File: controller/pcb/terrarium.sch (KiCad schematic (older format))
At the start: 72 parts, among them K1 G3MB-202P, K2 G3MB-202P, K3 G3MB-202P, P1 USB_C_Plug_USB2.0, Q1 S8050, Q2 S8050, Q3 S8050, Q4 S8050, SW1 RESET, SW3 RTC BATTERY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

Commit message: update footprints, move rx/tx leds
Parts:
- removed R12: 5k, Resistor_SMD:R_1206_3216Metric, symbol Device:R_Small
- removed SW3: RTC BATTERY, Button_Switch_SMD:SW_DIP_SPSTx01_Slide_6.7x4.1mm_W6.73mm_P2.54mm_LowProfile_JPin, symbol Switch:SW_Push
- LED4: value POWER -> PWR
- LED5: value SENS -> SNS
- R12: renamed from R19; value 10k -> 3k
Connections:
- wire segments 211 -> 205
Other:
- moved on the sheet: LED4, LED6, LED7, R12
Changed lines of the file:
@@
 Wire Wire Line
 	4350 4600 4250 4600
-$Comp
-L Mechanical:MountingHole H1
-U 1 1 61A0FEAA
-P 900 6300
-F 0 "H1" H 1000 6300 50  0000 L CNN
-F 1 "MountingHole" H 1000 6255 50  0001 L CNN
-F 2 "MountingHole:MountingHole_3.2mm_M3_Pad_Via" H 900 6300 50  0001 C CNN
-F 3 "~" H 900 6300 50  0001 C CNN
-	1    900  6300
-	1    0    0    -1
-$EndComp
-$Comp
-L Mechanical:MountingHole H2
-U 1 1 61A115E3
-P 1300 6300
-F 0 "H2" H 1400 6300 50  0000 L CNN
-F 1 "MountingHole" H 1400 6255 50  0001 L CNN
-F 2 "MountingHole:MountingHole_3.2mm_M3_Pad_Via" H 1300 6300 50  0001 C CNN
-F 3 "~" H 1300 6300 50  0001 C CNN
-	1    1300 6300
-	1    0    0    -1
-$EndComp
-$Comp
-L Mechanical:MountingHole H3
-U 1 1 61A11970
-P 1700 6300
-F 0 "H3" H 1800 6300 50  0000 L CNN
-F 1 "MountingHole" H 1800 6255 50  0001 L CNN
-F 2 "MountingHole:MountingHole_3.2mm_M3_Pad_Via" H 1700 6300 50  0001 C CNN
-F 3 "~" H 1700 6300 50  0001 C CNN
-	1    1700 6300
-	1    0    0    -1
-$EndComp
-$Comp
-L Mechanical:MountingHole H4
-U 1 1 61A11DAB
-P 2100 6300
-F 0 "H4" H 2200 6300 50  0000 L CNN
-F 1 "MountingHole" H 2200 6255 50  0001 L CNN
-F 2 "MountingHole:MountingHole_3.2mm_M3_Pad_Via" H 2100 6300 50  0001 C CNN
-F 3 "~" H 2100 6300 50  0001 C CNN
-	1    2100 6300
-	1    0    0    -1
-$EndComp
-Text Notes 700  6050 0    50   ~ 0
-Mount holes
 Text Notes 3050 650  0    50   ~ 0
 Relays
@@
 	1    0    0    -1
 $EndComp
-Wire Wire Line
-	10100 5500 10400 5500
 Wire Wire Line
 	11000 6750 10100 6750
@@
 $EndComp
 $Comp
-L Switch:SW_Push SW3
-U 1 1 61C4BD91
-P 10600 5500
-F 0 "SW3" H 10600 5785 50  0000 C CNN
-F 1 "RTC BATTERY" H 10600 5694 50  0000 C CNN
-F 2 "Button_Switch_SMD:SW_DIP_SPSTx01_Slide_6.7x4.1mm_W6.73mm_P2.54mm_LowProfile_JPin" H 10600 5700 50  0001 C CNN
-F 3 "~" H 10600 5700 50  0001 C CNN
-	1    10600 5500
-	1    0    0    -1
-$EndComp
-$Comp
 L Device:Q_NPN_BEC Q3
 U 1 1 61BD2EC2
@@
 G33
 Wire Wire Line
-	10800 5500 11000 5500
-Wire Wire Line
 	11000 5500 11000 5800
 Wire Wire Line
@@
 Connection ~ 10100 5500
 Wire Notes Line
-	700  6100 700  6500
-Wire Notes Line
-	700  6500 2400 6500
-Wire Notes Line
-	2400 6500 2400 6100
-Wire Notes Line
-	700  6100 2400 6100
-Wire Notes Line
 	700  6800 2200 6800
 Wire Notes Line
@@
 	2200 8150 700  8150
 Wire Notes Line
-	8450 4700 8450 700
+	7700 4700 7700 700
 Text Notes 8450 650  0    50   ~ 0
 ESP32 WROOM 32
@@
 $EndComp
 Wire Wire Line
-	4550 9100 4550 9400
-Connection ~ 4550 9100
-Connection ~ 3850 9100
-Wire Wire Line
-	3850 9100 4550 9100
-Wire Wire Line
-	4250 9950 4550 9950
-Wire Wire Line
-	4550 9000 4550 9100
-Wire Wire Line
-	3850 9950 4050 9950
-Connection ~ 3850 9950
-Wire Wire Line
 	3850 9600 3850 9950
-Wire Wire Line
-	4550 9950 4550 9700
 Wire Wire Line
 	3300 9950 3850 9950
@@
 L power:+3V3 #PWR010
 U 1 1 61CB24C1
-P 4550 9000
-F 0 "#PWR010" H 4550 8850 50  0001 C CNN
-F 1 "+3V3" H 4565 9173 50  0000 C CNN
-F 2 "" H 4550 9000 50  0001 C CNN
-F 3 "" H 4550 9000 50  0001 C CNN
-	1    4550 9000
+P 3850 9100
+F 0 "#PWR010" H 3850 8950 50  0001 C CNN
+F 1 "+3V3" H 3865 9273 50  0000 C CNN
+F 2 "" H 3850 9100 50  0001 C CNN
+F 3 "" H 3850 9100 50  0001 C CNN
+	1    3850 9100
 	-1   0    0    -1
 $EndComp
@@
 L Device:LED LED4
 U 1 1 61C6039A
-P 4550 9550
-F 0 "LED4" H 4650 9450 50  0000 R CNN
-F 1 "POWER" H 4650 9650 50  0000 R CNN
-F 2 "LED_SMD:LED_1206_3216Metric" H 4550 9550 50  0001 C CNN
-F 3 "~" H 4550 9550 50  0001 C CNN
-	1    4550 9550
-	0    -1   -1   0
-$EndComp
-$Comp
-L Device:R_Small R12
-U 1 1 61C5EFC3
-P 4150 9950
-F 0 "R12" V 4250 9950 50  0000 C CNN
-F 1 "5k" V 4050 9950 50  0000 C CNN
-F 2 "Resistor_SMD:R_1206_3216Metric" H 4150 9950 50  0001 C CNN
-F 3 "~" H 4150 9950 50  0001 C CNN
-	1    4150 9950
+P 8300 3200
+F 0 "LED4" H 8400 3100 50  0000 R CNN
+F 1 "PWR" H 8400 3300 50  0000 R CNN
+F 2 "LED_SMD:LED_1206_3216Metric" H 8300 3200 50  0001 C CNN
+F 3 "~" H 8300 3200 50  0001 C CNN
+	1    8300 3200
 	0    -1   -1   0
 $EndComp
@@
 P 8650 8150
 F 0 "LED5" H 8750 8050 50  0000 R CNN
-F 1 "SENS" H 8750 8250 50  0000 R CNN
+F 1 "SNS" H 8750 8250 50  0000 R CNN
 F 2 "LED_SMD:LED_1206_3216Metric" H 8650 8150 50  0001 C CNN
 F 3 "~" H 8650 8150 50  0001 C CNN
@@
 L Device:LED LED6
 U 1 1 6243730D
-P 8700 2500
-F 0 "LED6" H 8800 2400 50  0000 R CNN
-F 1 "RX" H 8800 2600 50  0000 R CNN
-F 2 "LED_SMD:LED_1206_3216Metric" H 8700 2500 50  0001 C CNN
-F 3 "~" H 8700 2500 50  0001 C CNN
-	1    8700 2500
+P 9100 3200
+F 0 "LED6" H 9200 3100 50  0000 R CNN
+F 1 "RX" H 9200 3300 50  0000 R CNN
+F 2 "LED_SMD:LED_1206_3216Metric" H 9100 3200 50  0001 C CNN
+F 3 "~" H 9100 3200 50  0001 C CNN
+	1    9100 3200
 	0    -1   -1   0
 $EndComp
@@
 L Device:LED LED7
 U 1 1 62438D58
-P 9100 2500
-F 0 "LED7" H 9200 2400 50  0000 R CNN
-F 1 "TX" H 9200 2600 50  0000 R CNN
-F 2 "LED_SMD:LED_1206_3216Metric" H 9100 2500 50  0001 C CNN
-F 3 "~" H 9100 2500 50  0001 C CNN
-	1    9100 2500
-	0    -1   -1   0
-$EndComp
-Text GLabel 8700 2350 1    50   Input ~ 0
+P 8700 3200
+F 0 "LED7" H 8800 3100 50  0000 R CNN
+F 1 "TX" H 8800 3300 50  0000 R CNN
+F 2 "LED_SMD:LED_1206_3216Metric" H 8700 3200 50  0001 C CNN
+F 3 "~" H 8700 3200 50  0001 C CNN
+	1    8700 3200
+	0    -1   -1   0
+$EndComp
+Text GLabel 9100 3350 3    50   Input ~ 0
 RX
-Text GLabel 9100 2350 1    50   Input ~ 0
+Text GLabel 8700 3350 3    50   Input ~ 0
 TX
 Wire Wire Line
-	8700 2650 8700 2850
-Wire Wire Line
-	8700 2850 8900 2850
-Wire Wire Line
-	9100 2850 9100 2650
-$Comp
-L Device:R_Small R19
+	9100 3050 9100 2850
+Wire Wire Line
+	8700 2850 8700 3050
+$Comp
+L Device:R_Small R12
 U 1 1 624CEFE7
-P 8900 3050
-F 0 "R19" V 9000 3050 50  0000 C CNN
-F 1 "10k" V 8800 3050 50  0000 C CNN
-F 2 "Resistor_SMD:R_1206_3216Metric" H 8900 3050 50  0001 C CNN
-F 3 "~" H 8900 3050 50  0001 C CNN
-	1    8900 3050
-	-1   0    0    1
-$EndComp
-Wire Wire Line
-	8900 2950 8900 2850
-Connection ~ 8900 2850
-Wire Wire Line
-	8900 2850 9100 2850
-$Comp
-L power:GND #PWR023
-U 1 1 624FB737
-P 8900 3300
-F 0 "#PWR023" H 8900 3050 50  0001 C CNN
-F 1 "GND" H 8905 3127 50  0000 C CNN
-F 2 "" H 8900 3300 50  0001 C CNN
-F 3 "" H 8900 3300 50  0001 C CNN
-	1    8900 3300
-	1    0    0    -1
-$EndComp
-Wire Wire Line
-	8900 3300 8900 3150
+P 8700 2650
+F 0 "R12" V 8800 2650 50  0000 C CNN
+F 1 "3k" V 8600 2650 50  0000 C CNN
+F 2 "Resistor_SMD:R_1206_3216Metric" H 8700 2650 50  0001 C CNN
+F 3 "~" H 8700 2650 50  0001 C CNN
+	1    8700 2650
+	1    0    0    -1
+$EndComp
+Wire Wire Line
+	8700 2750 8700 2850
+Wire Wire Line
+	8700 2400 8700 2550
+$Comp
+L power:+3V3 #PWR0101
+U 1 1 61EFC8AF
+P 8700 2400
+F 0 "#PWR0101" H 8700 2250 50  0001 C CNN
+F 1 "+3V3" H 8715 2573 50  0000 C CNN
+F 2 "" H 8700 2400 50  0001 C CNN
+F 3 "" H 8700 2400 50  0001 C CNN
+	1    8700 2400
+	-1   0    0    -1
+$EndComp
+Wire Wire Line
+	10100 5500 11000 5500
+Connection ~ 3850 9100
+Wire Wire Line
+	8700 2850 8300 2850
+Wire Wire Line
+	8300 2850 8300 3050
+Connection ~ 8700 2850
+$Comp
+L power:GND #PWR0102
+U 1 1 62065A46
+P 8300 3350
+F 0 "#PWR0102" H 8300 3100 50  0001 C CNN
+F 1 "GND" H 8305 3177 50  0000 C CNN
+F 2 "" H 8300 3350 50  0001 C CNN
+F 3 "" H 8300 3350 50  0001 C CNN
+	1    8300 3350
+	1    0    0    -1
+$EndComp
+Wire Wire Line
+	8700 2850 9100 2850
+Wire Notes Line
+	700  6100 2400 6100
+Wire Notes Line
+	2400 6500 2400 6100
+Wire Notes Line
+	700  6500 2400 6500
+Wire Notes Line
+	700  6100 700  6500
+Text Notes 700  6050 0    50   ~ 0
+Mount holes
+$Comp
+L Mechanical:MountingHole H4
+U 1 1 61A11DAB
+P 2100 6300
+F 0 "H4" H 2200 6300 50  0000 L CNN
+F 1 "MountingHole" H 2200 6255 50  0001 L CNN
+F 2 "MountingHole:MountingHole_3.2mm_M3_Pad_Via" H 2100 6300 50  0001 C CNN
+F 3 "~" H 2100 6300 50  0001 C CNN
+	1    2100 6300
+	1    0    0    -1
+$EndComp
+$Comp
+L Mechanical:MountingHole H3
+U 1 1 61A11970
+P 1700 6300
+F 0 "H3" H 1800 6300 50  0000 L CNN
+F 1 "MountingHole" H 1800 6255 50  0001 L CNN
+F 2 "MountingHole:MountingHole_3.2mm_M3_Pad_Via" H 1700 6300 50  0001 C CNN
+F 3 "~" H 1700 6300 50  0001 C CNN
+	1    1700 6300
+	1    0    0    -1
+$EndComp
+$Comp
+L Mechanical:MountingHole H2
+U 1 1 61A115E3
+P 1300 6300
+F 0 "H2" H 1400 6300 50  0000 L CNN
+F 1 "MountingHole" H 1400 6255 50  0001 L CNN
+F 2 "MountingHole:MountingHole_3.2mm_M3_Pad_Via" H 1300 6300 50  0001 C CNN
+F 3 "~" H 1300 6300 50  0001 C CNN
+	1    1300 6300
+	1    0    0    -1
+$EndComp
+$Comp
+L Mechanical:MountingHole H1
+U 1 1 61A0FEAA
+P 900 6300
+F 0 "H1" H 1000 6300 50  0000 L CNN
+F 1 "MountingHole" H 1000 6255 50  0001 L CNN
+F 2 "MountingHole:MountingHole_3.2mm_M3_Pad_Via" H 900 6300 50  0001 C CNN
+F 3 "~" H 900 6300 50  0001 C CNN
+	1    900  6300
+	1    0    0    -1
+$EndComp
 $EndSCHEMATC

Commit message: add cp2102
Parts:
- removed C2: 10uF, Capacitor_SMD:C_1206_3216Metric, symbol Device:C_Small
- removed C3: 47uF, Capacitor_SMD:C_1206_3216Metric, symbol Device:C_Small
- removed LED5: SNS, LED_SMD:LED_1206_3216Metric, symbol Device:LED
- removed P1: USB_C_Plug_USB2.0, Connector_USB:USB_C_Receptacle_Palconn_UTC16-G, symbol Connector:USB_C_Plug_USB2.0
- removed Q4: S8050, Package_TO_SOT_SMD:SOT-23, symbol Device:Q_NPN_BEC
- removed R10: 150ohm, Resistor_SMD:R_1206_3216Metric, symbol Device:R_Small
- removed R17: 5k, Resistor_SMD:R_1206_3216Metric, symbol Device:R_Small
- removed R18: 1M, Resistor_SMD:R_1206_3216Metric, symbol Device:R_Small
- removed RESET_j1: data, Connector_PinHeader_2.54mm:PinHeader_1x02_P2.54mm_Vertical, symbol Connector_Generic:Conn_01x02
- removed SENS1, SENS2, SENS6: 4, Connector_JST:JST_XH_B3B-XH-AM_1x03_P2.50mm_Vertical, symbol Connector_Generic_MountingPin:Conn_01x03_MountingPin
- removed SENS3: 1, Connector_JST:JST_XH_B3B-XH-AM_1x03_P2.50mm_Vertical, symbol Connector_Generic_MountingPin:Conn_01x03_MountingPin
- removed SENS4: 2, Connector_JST:JST_XH_B3B-XH-AM_1x03_P2.50mm_Vertical, symbol Connector_Generic_MountingPin:Conn_01x03_MountingPin
- removed SENS5: 3, Connector_JST:JST_XH_B3B-XH-AM_1x03_P2.50mm_Vertical, symbol Connector_Generic_MountingPin:Conn_01x03_MountingPin
- removed TP1, TP2: TestPoint, TestPoint:TestPoint_Pad_1.5x1.5mm, symbol Connector:TestPoint
- removed U3: LM1117-3.3, Package_TO_SOT_SMD:SOT-223-3_TabPin2, symbol Regulator_Linear:LM1117-3.3
- SW1: value RESET -> RST
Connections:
- wire segments 205 -> 140
- no-connect marks 29 -> 19
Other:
- note removed: "Power 3v3 and 5v"
- note removed: "Sensors"
- moved on the sheet: ALED1, BT1, C1, D4, H1, H2, H3, H4, LED4, LED6, LED7, R11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

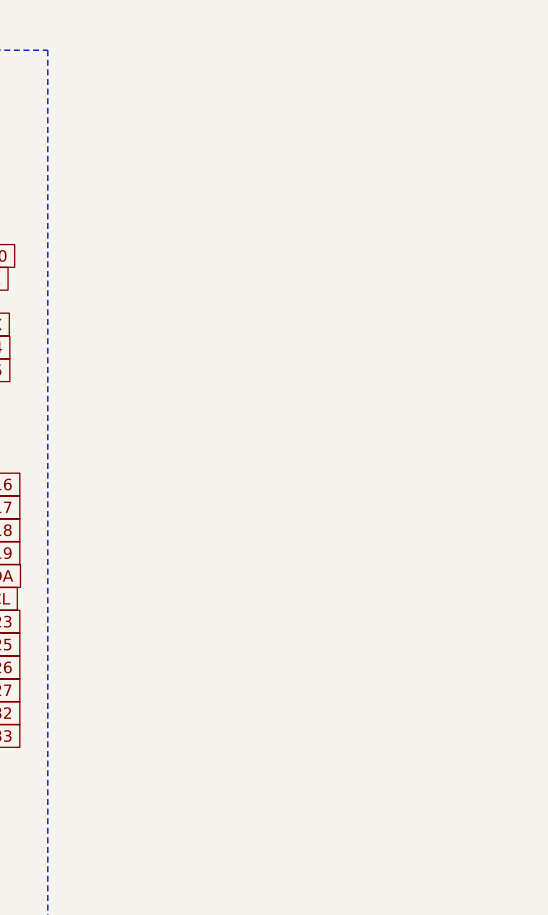
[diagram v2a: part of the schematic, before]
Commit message: add ground, 5v inner planes
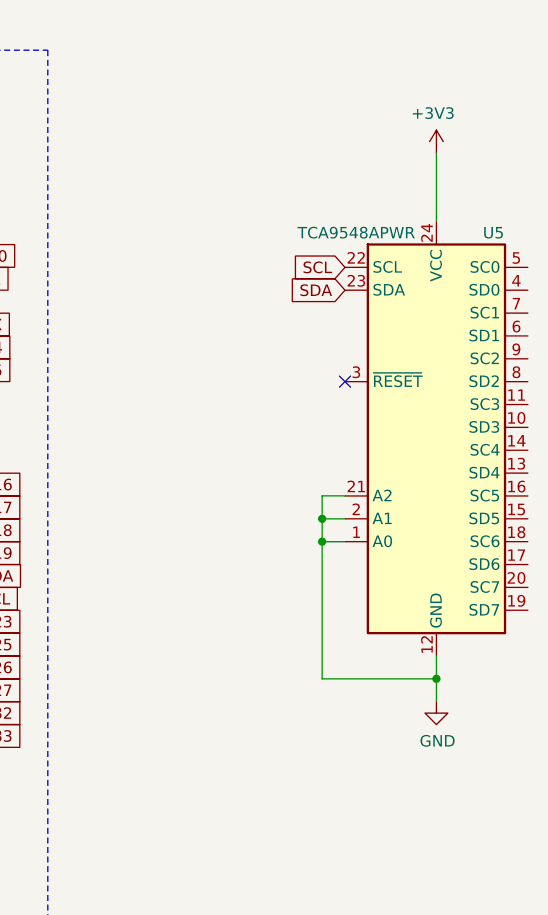
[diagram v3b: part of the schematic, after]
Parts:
- added U5: TCA9548APWR, Package_SO:TSSOP-24_4.4x7.8mm_P0.65mm, symbol Interface_Expansion:TCA9548APWR
- SW1: footprint Button_Switch_SMD:SW_DIP_SPSTx01_Slide_6.7x4.1mm_W6.73mm_P2.54mm_LowProfile_JPin -> Button_Switch_THT:SW_Tactile_SPST_Angled_PTS645Vx39-2LFS
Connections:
- net +3V3: now also U5.24 (VCC)
- net GND: now also U5.1 (A0), U5.12 (GND), U5.2 (A1), U5.21 (A2)
- net SCL: now also U5.22 (SCL)
- net SDA: now also U5.23 (SDA)
- no-connect marks 19 -> 20
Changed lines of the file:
@@
 F 0 "SW1" H 8400 2285 50  0000 C CNN
 F 1 "RST" H 8400 2194 50  0000 C CNN
-F 2 "Button_Switch_SMD:SW_DIP_SPSTx01_Slide_6.7x4.1mm_W6.73mm_P2.54mm_LowProfile_JPin" H 8400 2200 50  0001 C CNN
+F 2 "Button_Switch_THT:SW_Tactile_SPST_Angled_PTS645Vx39-2LFS" H 8400 2200 50  0001 C CNN
 F 3 "~" H 8400 2200 50  0001 C CNN
 	1    8400 2000
@@
 Wire Wire Line
 	8400 1500 8400 1800
+$Comp
+L Interface_Expansion:TCA9548APWR U5
+U 1 1 61EF247F
+P 12100 2350
+F 0 "U5" H 12350 3200 50  0000 C CNN
+F 1 "TCA9548APWR" H 11750 3200 50  0000 C CNN
+F 2 "Package_SO:TSSOP-24_4.4x7.8mm_P0.65mm" H 12100 1350 50  0001 C CNN
+F 3 "http://www.ti.com/lit/ds/symlink/tca9548a.pdf" H 12150 2600 50  0001 C CNN
+	1    12100 2350
+	1    0    0    -1
+$EndComp
+Text GLabel 11700 1750 0    50   Input ~ 0
+SDA
+Text GLabel 11700 1650 0    50   Input ~ 0
+SCL
+$Comp
+L power:GND #PWR029
+U 1 1 61EF526D
+P 12100 3550
+F 0 "#PWR029" H 12100 3300 50  0001 C CNN
+F 1 "GND" H 12105 3377 50  0000 C CNN
+F 2 "" H 12100 3550 50  0001 C CNN
+F 3 "" H 12100 3550 50  0001 C CNN
+	1    12100 3550
+	1    0    0    -1
+$EndComp
+Wire Wire Line
+	12100 3350 12100 3450
+Wire Wire Line
+	12100 3450 11600 3450
+Wire Wire Line
+	11600 3450 11600 2850
+Wire Wire Line
+	11600 2650 11700 2650
+Connection ~ 12100 3450
+Wire Wire Line
+	12100 3450 12100 3550
+Wire Wire Line
+	11700 2750 11600 2750
+Connection ~ 11600 2750
+Wire Wire Line
+	11600 2750 11600 2650
+Wire Wire Line
+	11700 2850 11600 2850
+Connection ~ 11600 2850
+Wire Wire Line
+	11600 2850 11600 2750
+NoConn ~ 11700 2150
+$Comp
+L power:+3V3 #PWR028
+U 1 1 61F1897D
+P 12100 1150
+F 0 "#PWR028" H 12100 1000 50  0001 C CNN
+F 1 "+3V3" H 12115 1323 50  0000 C CNN
+F 2 "" H 12100 1150 50  0001 C CNN
+F 3 "" H 12100 1150 50  0001 C CNN
+	1    12100 1150
+	-1   0    0    -1
+$EndComp
+Wire Wire Line
+	12100 1150 12100 1450
 $EndSCHEMATC
